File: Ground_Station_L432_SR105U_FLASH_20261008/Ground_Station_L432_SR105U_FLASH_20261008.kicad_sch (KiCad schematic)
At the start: 63 parts, among them J10 SC1464-ND, J11 SC1464-ND, J12 SQ, J13 Conn_01x12, J15 Conn_01x12, J7 SQ, J8 Conn_01x15, J9 Conn_01x15, SW1 SW_Push, SW2 MODE, SW3 SW_Push, SW4 SW_Coded, U1 SR105U, U3 MCP604, U4 W25Q128JVS

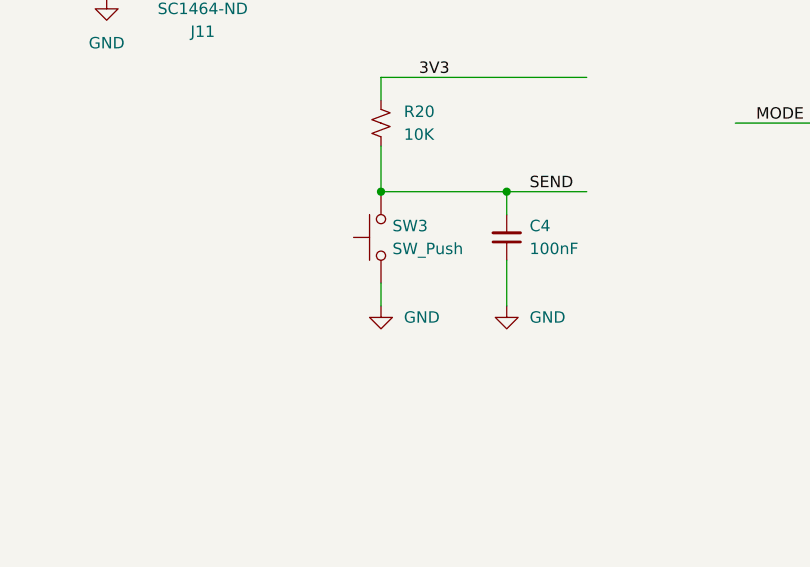
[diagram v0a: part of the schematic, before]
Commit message: Update PCB design. Replace Send button with larger one.
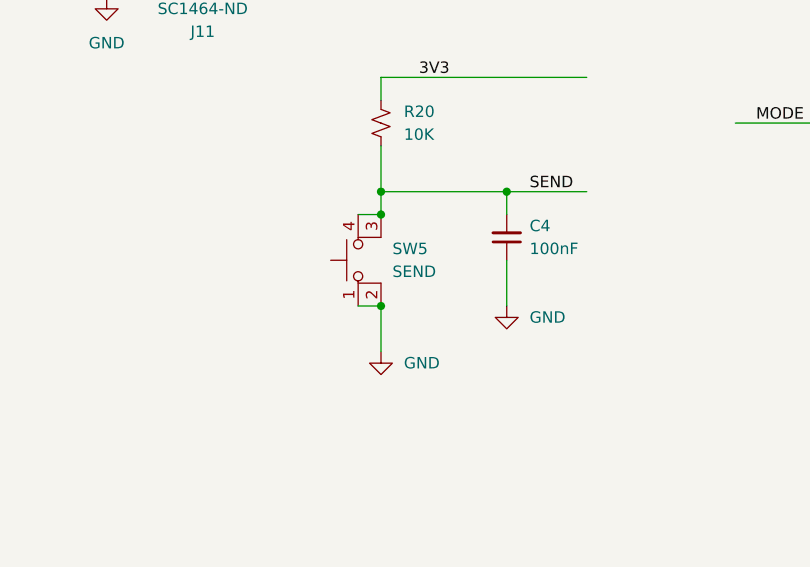
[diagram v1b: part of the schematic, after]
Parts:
- removed SW3: SW_Push, Button_Switch_THT:SW_PUSH_1P1T_6x3.5mm_H4.3_APEM_MJTP1243, symbol Switch:SW_Push
- added SW5: SEND, GroundStation:SW_PUSH-12mm, symbol Switch:SW_MEC_5E
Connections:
- net GND: now also SW5.1, SW5.2
- net SEND: now also SW5.3 (K), SW5.4 (A)

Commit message: Change name of SW1 to RESET
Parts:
- SW1: value SW_Push -> RESET
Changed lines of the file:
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@@
 			)
 		)
-		(property "Value" "SW_Push"
+		(property "Value" "RESET"
 			(at 72.39 218.4399 90)
 			(show_name no)
